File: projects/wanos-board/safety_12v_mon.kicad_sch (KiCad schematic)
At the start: 4 parts, among them U4 PC817A

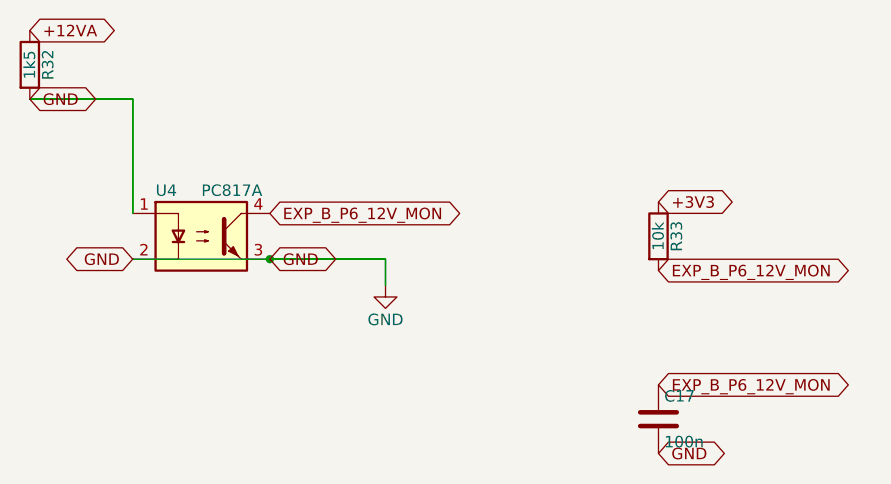
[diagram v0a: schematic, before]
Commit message: pi_power & 12V_monitor schematics OK added datasheets doc update
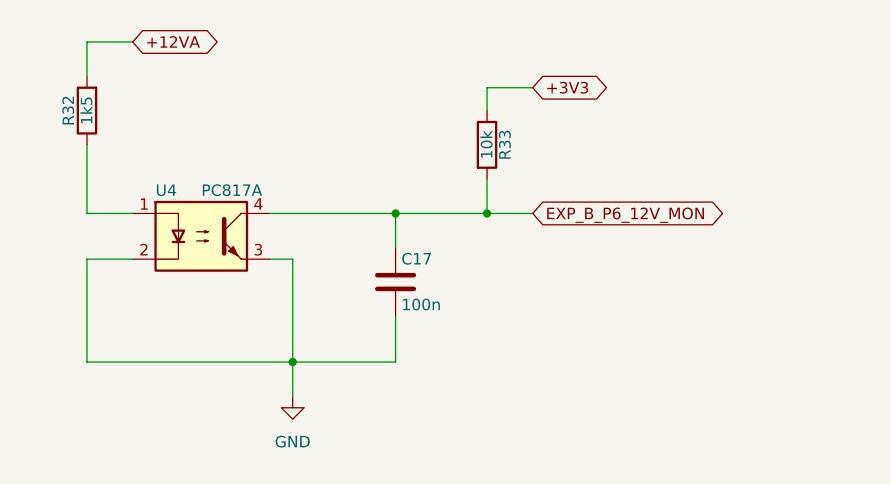
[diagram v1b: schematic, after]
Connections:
- net +12VA: now also R32.2; no longer R32.1
- net GND: no longer R32.2, U4.1
- new net: R32.1, U4.1
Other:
- moved on the sheet: C17, R32, R33
